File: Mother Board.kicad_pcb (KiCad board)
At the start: 2 copper layers, 236.2 x 139.7 mm, 120 parts, among them J1 Conn_01x04, J2 USB_B_Mini, J3 Conn_02x05_Odd_Even, J4 Conn_01x04, J5 Conn_01x03, J6 Conn_01x03, J7 Conn_01x04, SW1 SW_Push, U3 FT232RL, U4 STM32F407IGTx, U5 TPS2111APWR, Y1 Crystal_GND24

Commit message: worked on layout for power mux section
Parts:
- removed CARD2, CARD3, CARD5, CARD6, CARD7: Conn_02x22_Top_Bottom, connectors_mdg:5530843-4
- removed R44, R45, R46, R47, R48: 10k, Resistor_SMD:R_0603_1608Metric_Pad1.05x0.95mm_HandSolder
- removed the REF** at (89.2, 71.8)
- removed the REF** at (286.4, 151.8)
- removed the REF** at (258.4, 151.8)
- removed the REF** at (230.5, 151.8)
- removed the REF** at (202.6, 151.8)
- removed the REF** at (118.7, 71.8)
- removed the REF** at (314.3, 71.8)
- removed the REF** at (286.4, 71.8)
- removed the REF** at (258.4, 71.8)
- removed the REF** at (230.5, 71.8)
- removed the REF** at (202.6, 71.8)
- removed the REF** at (314.3, 151.8)
- added C27: 0.1uF, Capacitor_SMD:C_0603_1608Metric_Pad1.05x0.95mm_HandSolder, F.Cu at (133.1, 184.7)
- added C28: 0.1uF, Capacitor_SMD:C_0603_1608Metric_Pad1.05x0.95mm_HandSolder, F.Cu at (130.4, 193.2)
- added D1: LED, LED_SMD:LED_1206_3216Metric_Pad1.42x1.75mm_HandSolder, F.Cu at (107.8, 201.2)
- added D2: LED, LED_SMD:LED_1206_3216Metric_Pad1.42x1.75mm_HandSolder, F.Cu at (101.5, 201.2)
- added L1: L, Inductor_SMD:L_1206_3216Metric, F.Cu at (94.0, 176.0)
- added R10: 0R, Resistor_SMD:R_0603_1608Metric_Pad1.05x0.95mm_HandSolder, F.Cu at (100.0, 177.0)
- added R11: 0R, Resistor_SMD:R_0603_1608Metric_Pad1.05x0.95mm_HandSolder, F.Cu at (100.0, 175.0)
- added R12: 23.7K, Resistor_SMD:R_0603_1608Metric_Pad1.05x0.95mm_HandSolder, F.Cu at (103.2, 162.5)
- added U1: SC189, Package_TO_SOT_SMD:SOT-23-5_HandSoldering, F.Cu at (89.3, 176.1)
- added U2: TPS2121, packages_mdg:Texas_VQFN_HR_12, F.Cu at (103.2, 157.4)
- added U6: W25Q128JV-DTR, Package_SO:SOIC-8_3.9x4.9mm_P1.27mm, F.Cu at (154.8, 168.8)
- C18: value 0.1uF -> CP; footprint Capacitor_SMD:C_0603_1608Metric_Pad1.05x0.95mm_HandSolder -> Capacitor_THT:CP_Radial_D8.0mm_P3.50mm
- C19: value 0.1uF -> 10uF
- C21: value 0.1uF -> 22uF
- C22, C23: value 0.1uF -> 1uF
- C24, C25: value 0.1uF -> 2.2uF
- C9: value 0.1uF -> 4.7uF
- R1, R2: value R -> 330R
- R19, R21, R23, R32, R34: value 10k -> 5K
- R20, R24: value 10k -> 13.7K
- R22: value 10k -> 23.7K
- R33: value 10k -> 10.2K
- R35, R36: value 10k -> 10K
- R37, R38: value 10k -> 330R
- R39, R40: value 10k -> 20K
- U4: value STM32F407IGTx -> TPS2121; footprint Package_QFP:LQFP-176_24x24mm_P0.5mm -> packages_mdg:Texas_VQFN_HR_12
- U5: value TPS2111APWR -> STM32F407VGTx; footprint Package_SO:TSSOP-8_4.4x3mm_P0.65mm -> Package_QFP:LQFP-100_14x14mm_P0.5mm
- Y1: footprint Crystals:Crystal_SMD_SeikoEpson_TSX3225-4pin_3.2x2.5mm -> Crystal:Crystal_SMD_SeikoEpson_TSX3225-4Pin_3.2x2.5mm_HandSoldering
- moved TP6 221.0 mm to (99.0, 69.5)
- moved R20 180.2 mm to (91.0, 162.3), turned to 180 degrees
- moved R21 178.2 mm to (91.0, 164.2), turned to 0 degrees
- moved TP1 173.2 mm to (154.5, 79.2)
- moved TP5 172.8 mm to (159.5, 79.2)
- moved TP7 172.1 mm to (164.5, 79.2)
- moved TP9 171.5 mm to (164.5, 73.0)
- moved TP2 171.2 mm to (159.5, 73.2)
- moved TP8 168.7 mm to (164.5, 67.2)
- moved TP4 168.4 mm to (154.6, 73.2)
- moved R19 168.1 mm to (103.2, 164.2), turned to 0 degrees
- moved R24 153.6 mm to (87.2, 162.3), turned to 0 degrees
- moved R22 145.8 mm to (99.5, 162.5), turned to 0 degrees
- moved R23 144.9 mm to (99.5, 164.2), turned to 180 degrees
- moved TP3 144.9 mm to (186.8, 73.0)
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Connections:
- C1 pad 1: Net-(C1-Pad1) -> 5V_EXT
- C10 pad 2: +3V3 -> /USB_VBUS
- C17 pad 1: Net-(C17-Pad1) -> 3V3_EXT
- C18 pad 1: +3V3 -> 3V3_EXT
- C19 pad 1: +3V3 -> GND
- C19 pad 2: GND -> /USB_VBUS
- C2 pad 1: Net-(C2-Pad1) -> +24V
- C2 pad 2: Net-(C2-Pad2) -> GND
- C20 pad 1: +3V3 -> Net-(C20-Pad1)
- C21 pad 1: +3V3 -> GND
- C21 pad 2: GND -> /3v3_REG_OUT
- C22 pad 1: +3V3 -> GND
- C22 pad 2: GND -> Net-(C22-Pad2)
- C23 pad 1: +3V3 -> GND
- C23 pad 2: GND -> Net-(C23-Pad2)
- C24 pad 1: +3V3 -> GND
- C24 pad 2: GND -> Net-(C24-Pad2)
- C25 pad 1: +3V3 -> GND
- C25 pad 2: GND -> Net-(C25-Pad2)
- C26 pad 1: +3V3 -> GND
- C26 pad 2: GND -> +3V3
- C3 pad 1: +3V3 -> 5V_EXT
- C4 pad 1: Net-(C4-Pad1) -> +24V
- C9 pad 2: +3V3 -> /USB_VBUS
- CARD0 pad 10: IC1_SDA -> I2C1_SCL
- CARD0 pad 31: SPI2_SCK -> SPI3_SCK
- CARD0 pad 32: SPI2_MISO -> SPI3_MISO
- CARD0 pad 33: SPI2_MOSI -> SPI3_MOSI
- CARD0 pad 9: IC1_SCL -> I2C1_SDA
- CARD1 pad 10: IC1_SDA -> I2C1_SCL
- CARD1 pad 16: USART6_TX -> USART2_TX
- CARD1 pad 17: USART6_RX -> USART2_RX
- CARD1 pad 18: USART6_CTS -> USART2_CTS
- CARD1 pad 19: USART6_RTS -> USART2_RTS
- CARD1 pad 31: SPI2_SCK_PI1 -> SPI3_SCK
- CARD1 pad 32: SPI2_MISO_PI2 -> SPI3_MISO
- CARD1 pad 33: SPI2_MOSI_PI3 -> SPI3_MOSI
- CARD1 pad 9: IC1_SCL -> I2C1_SDA
- CARD4 pad 10: IC1_SDA -> I2C1_SCL
- CARD4 pad 31: SPI2_SCK_PI1 -> SPI3_SCK
- CARD4 pad 32: SPI2_MISO_PI2 -> SPI3_MISO
- CARD4 pad 33: SPI2_MOSI_PI3 -> SPI3_MOSI
- CARD4 pad 39: CARD4_TIM12_CH1 -> CARD4_TIM12_CH2
- CARD4 pad 9: IC1_SCL -> I2C1_SDA
- J1 pad 1: GND -> 5V_EXT
- J1 pad 2: GND -> 5V_EXT
- J2 pad 1: Net-(C17-Pad1) -> /USB_VBUS
- J2 pad 2: Net-(J2-Pad2) -> /USB_D-
- J2 pad 3: Net-(J2-Pad3) -> /USB_D+
- J2 pad 5: Net-(J2-Pad5) -> GND
- J2 pad 6: Net-(J2-Pad6) -> GND
- J4 pad 3: +5V -> 3V3_EXT
- J4 pad 4: +5V -> 3V3_EXT
- J7 pad 3: +3V3 -> GND
- J7 pad 4: +3V3 -> GND
- R1 pad 1: +3V3 -> +5V
- R19 pad 1: /CARD2_ADD0 -> Net-(R12-Pad2)
- R2 pad 1: Net-(C4-Pad1) -> +3V3
- R20 pad 1: /CARD2_ADD1 -> 3V3_EXT
- R20 pad 2: +3V3 -> Net-(R20-Pad2)
- R21 pad 1: /CARD2_ADD2 -> Net-(R20-Pad2)
- R22 pad 1: /CARD3_ADD0 -> /USB_VBUS
- R22 pad 2: +3V3 -> Net-(R22-Pad2)
- R23 pad 1: /CARD3_ADD1 -> Net-(R22-Pad2)
- R23 pad 2: +3V3 -> GND
- R24 pad 1: /CARD3_ADD2 -> /3v3_REG_OUT
- R24 pad 2: GND -> Net-(R24-Pad2)
- R25 pad 1: USART2_RX_PD6 -> USART3_RX
- R26 pad 1: USART2_TX_PD5 -> USART3_TX
- R27 pad 1: USART2_CTS_PD3 -> USART3_CTS
- R28 pad 1: USART2_RTS_PD4 -> USART3_RTS
- R32 pad 1: /CARD5_ADD0 -> Net-(R24-Pad2)
- R32 pad 2: +3V3 -> GND
- R33 pad 1: /CARD5_ADD1 -> 5V_EXT
- R33 pad 2: GND -> Net-(R33-Pad2)
- R34 pad 1: /CARD5_ADD2 -> Net-(R33-Pad2)
- R34 pad 2: +3V3 -> GND
- R35 pad 1: /CARD6_ADD0 -> 3V3_EXT
- R35 pad 2: GND -> Net-(R35-Pad2)
- R36 pad 1: /CARD6_ADD1 -> Net-(R35-Pad2)
- R36 pad 2: +3V3 -> GND
- R37 pad 1: /CARD6_ADD2 -> Net-(D1-Pad1)
- R37 pad 2: +3V3 -> /TX_LED
- R38 pad 1: /CARD7_ADD0 -> Net-(D2-Pad1)
- R38 pad 2: +3V3 -> /RX_LED
- R39 pad 1: /CARD7_ADD1 -> GND
- R39 pad 2: +3V3 -> Net-(R39-Pad2)
- R40 pad 1: /CARD7_ADD2 -> GND
- R40 pad 2: +3V3 -> Net-(R40-Pad2)
- R8 pad 1: IC1_SDA -> I2C1_SDA
- R9 pad 1: IC1_SCL -> I2C1_SCL
- TP1 pad 1: SPI1_SCK -> IC1_SCL
- TP2 pad 1: SPI1_MISO -> IC1_SDA
- TP3 pad 1: SPI1_MOSI -> SPI3_SCK
- TP4 pad 1: IC1_SCL -> SPI3_MISO
- TP5 pad 1: IC1_SDA -> SPI3_MOSI
- U3 pad 15: Net-(U3-Pad15) -> /USB_D+
- U3 pad 16: Net-(U3-Pad16) -> /USB_D-
- U3 pad 17: Net-(U3-Pad17) -> Net-(C20-Pad1)
- U3 pad 18: Net-(U3-Pad18) -> GND
- U3 pad 19: Net-(U3-Pad19) -> +5V
- U3 pad 20: Net-(U3-Pad20) -> +5V
- U3 pad 21: Net-(U3-Pad21) -> GND
- U3 pad 22: Net-(U3-Pad22) -> /RX_LED
- U3 pad 23: Net-(U3-Pad23) -> /TX_LED
- U3 pad 25: Net-(U3-Pad25) -> GND
- U3 pad 26: Net-(U3-Pad26) -> GND
- U3 pad 4: Net-(U3-Pad4) -> +3V3
- U3 pad 7: Net-(U3-Pad7) -> GND
- U4 pad 1: Net-(U4-Pad1) -> +3V3
- U4 pad 10: Net-(U4-Pad10) -> Net-(R40-Pad2)
- U4 pad 11: Net-(U4-Pad11) -> Net-(C23-Pad2)
- U4 pad 12: Net-(U4-Pad12) -> GND
- U4 pad 2: Net-(U4-Pad2) -> /3v3_REG_OUT
- U4 pad 3: Net-(U4-Pad3) -> GND
- U4 pad 4: Net-(U4-Pad4) -> Net-(R24-Pad2)
- U4 pad 5: Net-(U4-Pad5) -> Net-(R20-Pad2)
- U4 pad 6: +3V3 -> Net-(R35-Pad2)
- U4 pad 7: Net-(U4-Pad7) -> 3V3_EXT
- U4 pad 8: Net-(U4-Pad8) -> +3V3
- U5 pad 1: Net-(U5-Pad1) -> CARD4_GPIO3
- U5 pad 2: Net-(U5-Pad2) -> CARD4_GPIO2
- U5 pad 3: Net-(U5-Pad3) -> CARD4_GPIO1
- U5 pad 4: Net-(U5-Pad4) -> CARD4_GPIO0
- U5 pad 5: GND -> Net-(U5-Pad5)
- U5 pad 6: Net-(C17-Pad1) -> +3V3
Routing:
- net +3V3: track 0.00 -> 197.1 mm, vias 0 -> 23
- net I2C1_SDA: track 0.00 -> 168.7 mm
- net I2C1_SCL: track 0.00 -> 162.8 mm
- net SPI3_SCK: track 0.00 -> 150.8 mm
- net SPI3_MISO: track 0.00 -> 148.9 mm
- net SPI3_MOSI: track 0.00 -> 131.2 mm
- net GND: track 0.00 -> 96.0 mm, vias 0 -> 49
- net USART2_RTS: track 0.00 -> 74.5 mm
- net USART2_RX: track 0.00 -> 74.3 mm
- net USART1_TX: track 0.00 -> 71.4 mm
- net USART1_RX: track 0.00 -> 67.9 mm
- net USART2_TX: track 0.00 -> 66.0 mm
- net USART1_CTS: track 0.00 -> 64.4 mm
- net USART1_RTS: track 0.00 -> 62.7 mm
- net USART2_CTS: track 0.00 -> 59.9 mm
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- added copper zone on In2.Cu, net +24V
- added copper zone on F.Cu, net +3V3
- added copper zone on In2.Cu, net +3V3
- added copper zone on F.Cu, net +5V
- added copper zone on In2.Cu, net +5V
- added copper zone on F.Cu, net /3v3_REG_OUT
- added copper zone on F.Cu, net /USB_VBUS
- added copper zone on F.Cu, net 3V3_EXT
- added copper zone on F.Cu, net 5V_EXT
- added copper zone on F.Cu, net GND
- added copper zone on In1.Cu, net GND
- added copper zone on F.Cu, net Net-(L1-Pad2)
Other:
- board size 236.2 x 139.7 mm -> 109 x 141 mm
- copper layers 2 -> 4

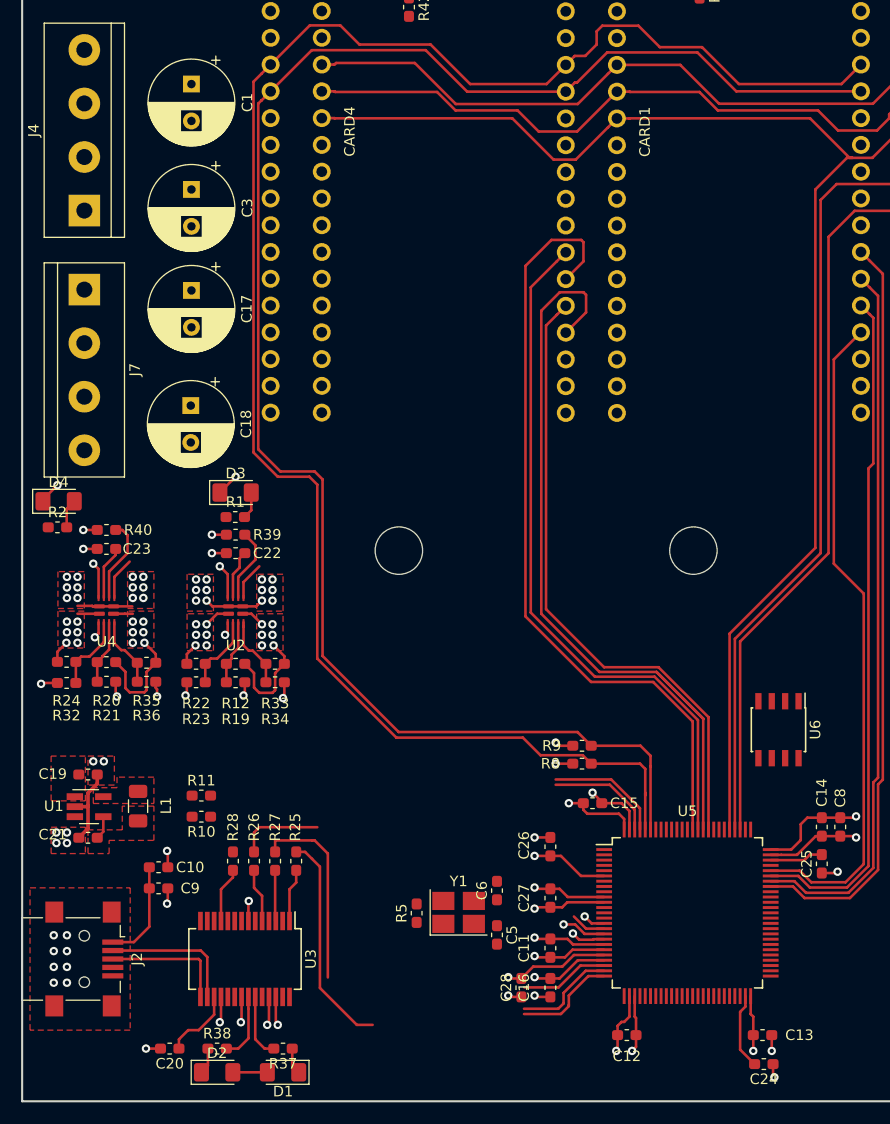
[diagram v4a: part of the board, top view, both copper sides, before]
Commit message: worked on layout of power mux, added inverter to enable 3v3 regulator
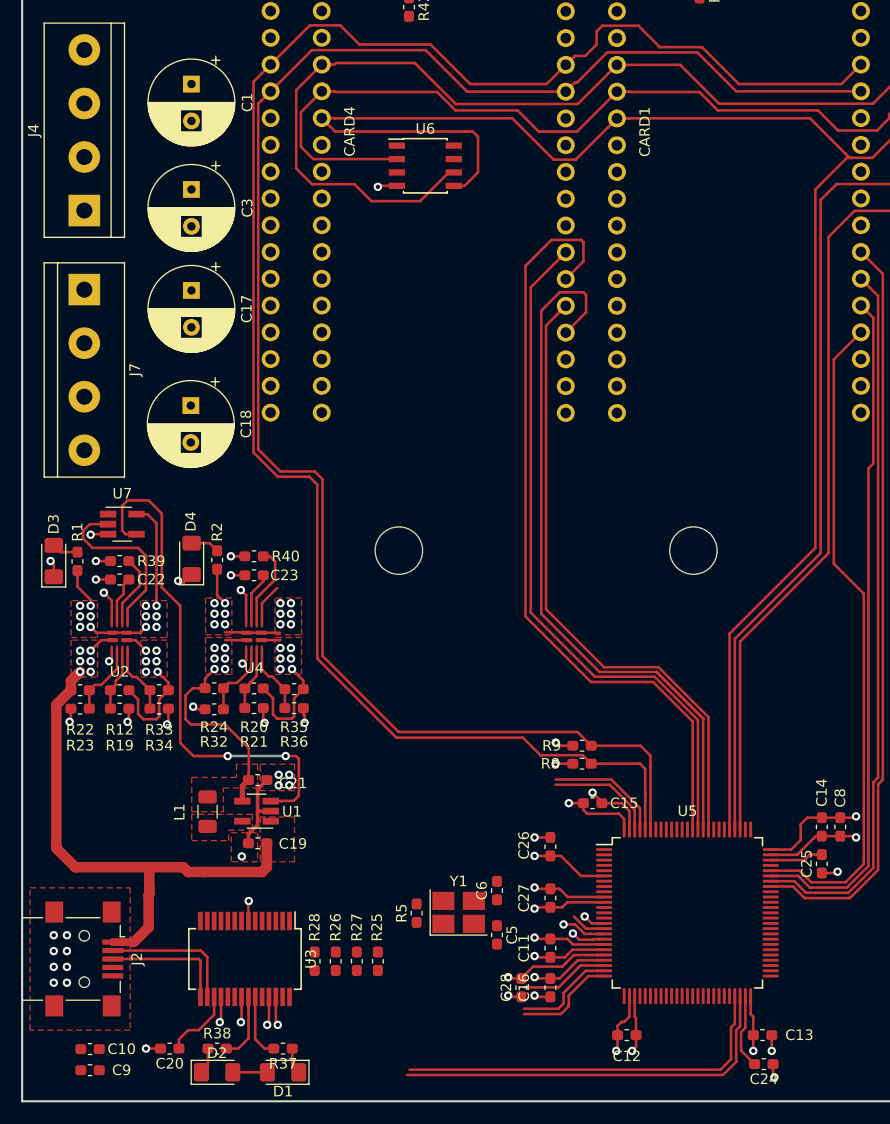
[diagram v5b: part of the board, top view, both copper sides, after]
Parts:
- removed R10, R11: 0R, Resistor_SMD:R_0603_1608Metric_Pad1.05x0.95mm_HandSolder
- added U7: SN74LVC1G04DBVR, Package_TO_SOT_SMD:SOT-23-5_HandSoldering, F.Cu at (92.5, 149.2)
- moved U6 63.1 mm to (121.2, 115.2), turned to 0 degrees
- moved C10 18.4 mm to (89.4, 199.0)
- moved C9 18.4 mm to (89.4, 201.0)
- moved D3 18.4 mm to (86.0, 152.8), turned to 90 degrees
- moved C19 17.4 mm to (105.3, 179.5), turned to 0 degrees
- moved C21 17.0 mm to (105.3, 173.5), turned to 180 degrees
- moved U1 15.9 mm to (105.2, 176.5), turned to 180 degrees
- moved R1 15.5 mm to (88.2, 152.8), turned to 90 degrees
- moved R2 15.5 mm to (101.5, 152.7), turned to 90 degrees
- moved C23 14.2 mm to (105.0, 154.1)
- moved R20 14.2 mm to (105.0, 164.8)
- moved R21 14.2 mm to (105.0, 166.7)
- moved R24 14.2 mm to (101.2, 164.8)
- moved R32 14.2 mm to (101.2, 166.8)
- moved R35 14.2 mm to (108.8, 164.9)
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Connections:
- U1 pad 3: /3v3_REG_EN -> 3v3_REG_EN
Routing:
- net +3V3: track 197.1 -> 78.9 mm
- net 5V_EXT: track 12.2 -> 100.0 mm
- net 3V3_EXT: track 12.2 -> 85.7 mm
- net 3v3_REG_EN: track 0.00 -> 49.1 mm, vias 0 -> 2
- net /USB_VBUS: track 14.3 -> 53.2 mm
- net USART3_TX: track 8.05 -> 37.0 mm
- net SPI3_SCK: track 150.8 -> 179.0 mm
- net SPI3_MOSI: track 131.2 -> 153.2 mm
- net USART3_CTS: track 18.4 -> 0.00 mm
- net USART3_RX: track 20.8 -> 38.1 mm
- net SPI3_MISO: track 148.9 -> 164.6 mm
- net /3v3_REG_OUT: track 6.48 -> 21.1 mm
- net +5V: track 9.11 -> 23.1 mm
- net Net-(U2-Pad9): track 3.62 -> 17.2 mm
- net /FTDI_CTS: track 5.28 -> 0.00 mm
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- added copper zone on In2.Cu, net 5V_EXT
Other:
- net class EXT_PWR added: clearance 0.3, trace_width 1, via_dia 0.8, via_drill 0.4

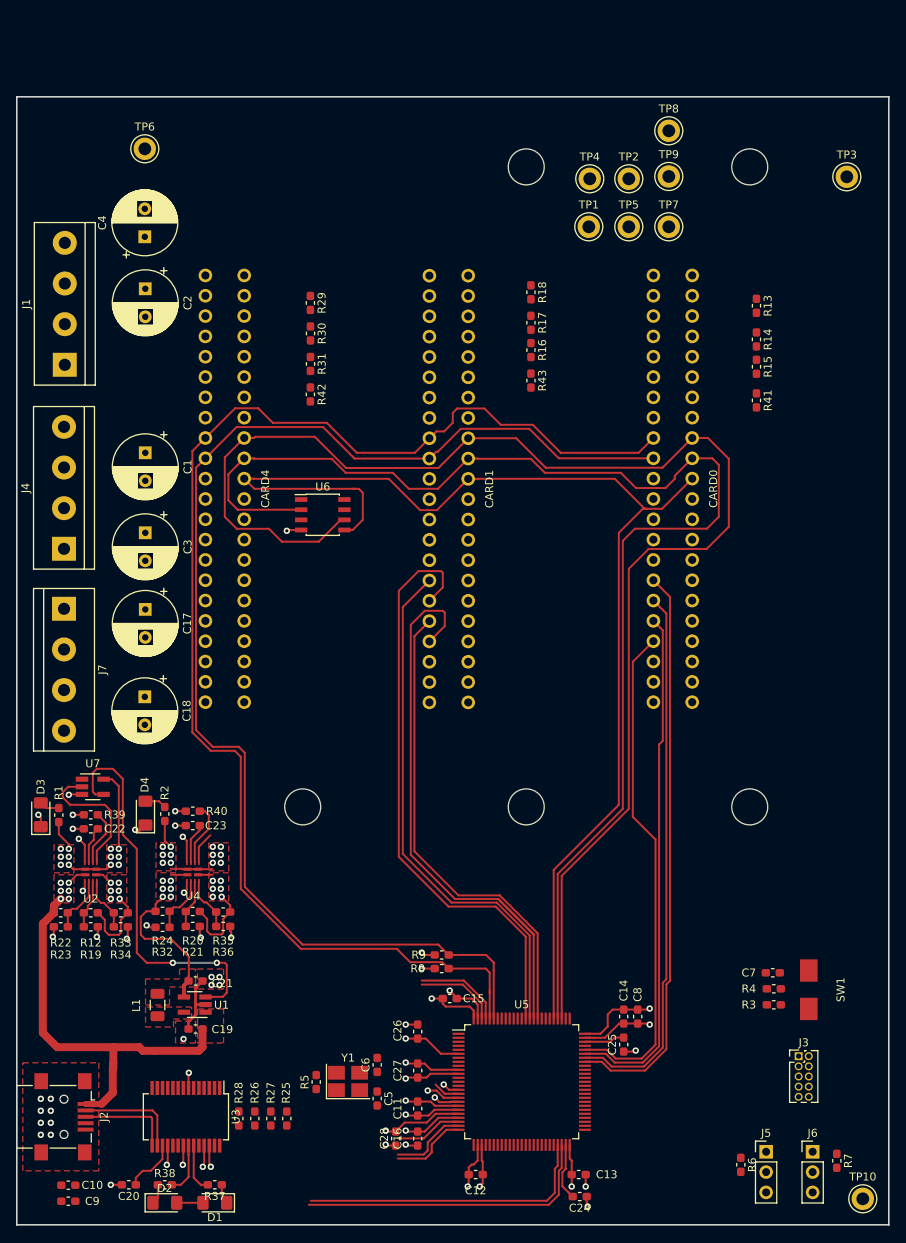
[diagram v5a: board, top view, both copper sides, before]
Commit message: all tracks connected, need to clean up layout before ordering.
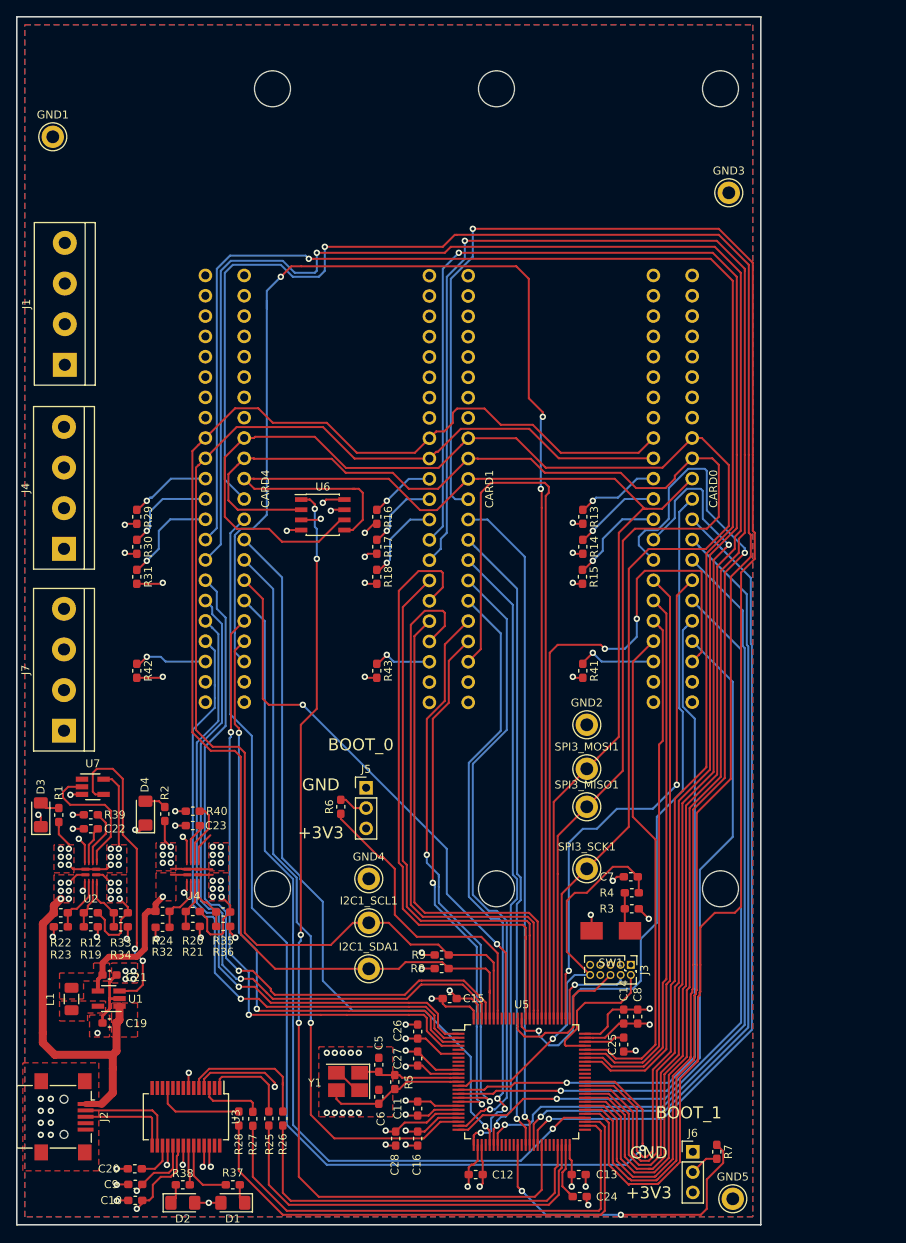
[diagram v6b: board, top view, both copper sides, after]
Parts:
- removed C1, C17, C18, C2, C3, C4: CP, Capacitor_THT:CP_Radial_D8.0mm_P3.50mm
- removed the REF** at (146.7, 71.8)
- removed the REF** at (174.6, 151.8)
- removed the REF** at (118.7, 151.8)
- removed TP1, TP10, TP2, TP3, TP4, TP5, TP6, TP7, TP8, TP9: TestPoint, Measurement_Points:Test_Point_Keystone_5010-5014_Multipurpose
- added GND1: TestPoint, test_points_mdg:Keystone_5010, F.Cu at (87.5, 68.0)
- added GND2: TestPoint, test_points_mdg:Keystone_5010, F.Cu at (154.2, 141.5)
- added GND3: TestPoint, test_points_mdg:Keystone_5010, F.Cu at (172.0, 75.0)
- added GND4: TestPoint, test_points_mdg:Keystone_5010, F.Cu at (127.0, 160.8)
- added GND5: TestPoint, test_points_mdg:Keystone_5010, F.Cu at (172.5, 200.8)
- added I2C1_SCL1: TestPoint, test_points_mdg:Keystone_5010, F.Cu at (127.0, 166.2)
- added I2C1_SDA1: TestPoint, test_points_mdg:Keystone_5010, F.Cu at (127.0, 172.0)
- added REF**: MountingHole_4.5mm, MountingHole:MountingHole_4.5mm, F.Cu at (143.0, 62.0)
- added REF**: MountingHole_4.5mm, MountingHole:MountingHole_4.5mm, F.Cu at (115.0, 62.0)
- added REF**: MountingHole_4.5mm, MountingHole:MountingHole_4.5mm, F.Cu at (171.0, 162.0)
- added REF**: MountingHole_4.5mm, MountingHole:MountingHole_4.5mm, F.Cu at (115.0, 162.0)
- added SPI3_MISO1: TestPoint, test_points_mdg:Keystone_5010, F.Cu at (154.2, 151.8)
- added SPI3_MOSI1: TestPoint, test_points_mdg:Keystone_5010, F.Cu at (154.2, 147.0)
- added SPI3_SCK1: TestPoint, test_points_mdg:Keystone_5010, F.Cu at (154.2, 159.5)
- moved J5 67.6 mm to (126.7, 149.4)
- moved R6 67.1 mm to (123.5, 151.8), turned to 90 degrees
- moved R43 41.1 mm to (128.0, 134.8)
- moved R42 40.8 mm to (98.0, 134.8)
- moved R18 40.4 mm to (128.0, 123.0)
- moved R41 40.2 mm to (153.8, 134.8)
- moved R29 34.4 mm to (98.0, 115.5)
- moved R30 34.4 mm to (98.0, 119.2)
- moved R31 34.3 mm to (98.0, 123.0)
- moved R13 34.2 mm to (153.8, 115.5)
- moved R15 34.1 mm to (153.7, 123.0)
- moved R17 34.0 mm to (128.0, 119.2)
- moved R14 33.8 mm to (153.8, 119.2)
- moved R16 28.4 mm to (128.0, 115.5)
- moved SW1 25.8 mm to (157.2, 167.2), turned to 0 degrees
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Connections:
- C10 pad 2: /USB_VBUS -> +5V
- C9 pad 2: /USB_VBUS -> +5V
- U5 pad 31: CARD0_TIM3_CH1 -> CARD1_TIM3_CH2
- U5 pad 32: CARD1_TIM3_CH2 -> CARD0_TIM3_CH1
- U5 pad 39: CARD0_TIM1_CH1N -> CARD1_TIM1_CH2N
- U5 pad 40: CARD0_TIM1_CH1 -> CARD1_TIM1_CH2
- U5 pad 41: CARD1_TIM1_CH2N -> CARD0_TIM1_CH1N
- U5 pad 42: CARD1_TIM1_CH2 -> CARD0_TIM1_CH1
- U5 pad 43: Net-(U5-Pad43) -> SPI_FLASH_CS
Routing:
- net CARD4_STATUS: track 0.00 -> 239.1 mm, vias 0 -> 1
- net CARD4_CS: track 0.00 -> 236.4 mm, vias 0 -> 1
- net CARD4_ENABLE: track 0.00 -> 229.4 mm, vias 0 -> 1
- net CARD1_STATUS: track 0.00 -> 211.2 mm, vias 0 -> 1
- net CARD1_CS: track 0.00 -> 211.2 mm, vias 0 -> 1
- net CARD1_ENABLE: track 0.00 -> 203.1 mm, vias 0 -> 1
- net CARD4_SENSE_NEG: track 0.00 -> 178.4 mm, vias 0 -> 3
- net CARD4_TIM8_CH1: track 0.00 -> 140.2 mm, vias 0 -> 1
- net CARD0_STATUS: track 0.00 -> 128.4 mm, vias 0 -> 1
- net SPI_FLASH_CS: track 0.00 -> 124.4 mm, vias 0 -> 4
- net CARD0_ENABLE: track 0.00 -> 114.7 mm, vias 0 -> 1
- net CARD4_TIM12_CH2: track 0.00 -> 108.7 mm, vias 0 -> 1
- net +5V: track 23.1 -> 125.3 mm, vias 12 -> 15
- net CARD0_TIM1_CH1: track 0.00 -> 100.9 mm, vias 0 -> 1
- net CARD0_TIM3_CH1: track 0.00 -> 99.6 mm, vias 0 -> 1
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- added copper zone on B.Cu, net GND
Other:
- board size 109 x 141 mm -> 93 x 151 mm
- board text added: "+3V3"
- board text added: "BOOT_0"
- board text added: "BOOT_1"
- board text added: "GND"
